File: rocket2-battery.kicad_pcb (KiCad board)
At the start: 4 copper layers, 142 parts, among them J1 Conn_01x07, J2 SMA, J3 ARM Cortex Debug, P1 PAD_SMD, P2 PAD_SMD, P3 PAD_SMD, P4 PAD_SMD, P5 PAD_SMD, P6 PAD_SMD, P7 PAD_SMD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

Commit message: Squished
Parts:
- U1: value ~ -> 3V3 LDO
- moved C26 14.6 mm to (127.9, 109.3)
- moved C27 14.6 mm to (131.5, 109.3)
- moved C28 14.6 mm to (135.4, 109.3)
- moved D15 14.6 mm to (139.3, 112.8)
- moved R46 14.6 mm to (136.3, 111.9)
- moved R47 14.6 mm to (130.3, 112.4)
- moved R49 14.6 mm to (132.2, 115.1)
- moved R50 14.6 mm to (143.2, 112.8)
- moved U14 14.6 mm to (113.8, 112.8)
- moved U15 14.6 mm to (133.2, 111.7)
- moved D16 14.6 mm to (139.3, 111.0)
- moved JP6 14.6 mm to (137.9, 115.7)
- moved R48 14.6 mm to (127.9, 113.2)
- moved R51 14.6 mm to (143.1, 111.0)
- moved D14 12.5 mm to (139.3, 100.1)
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
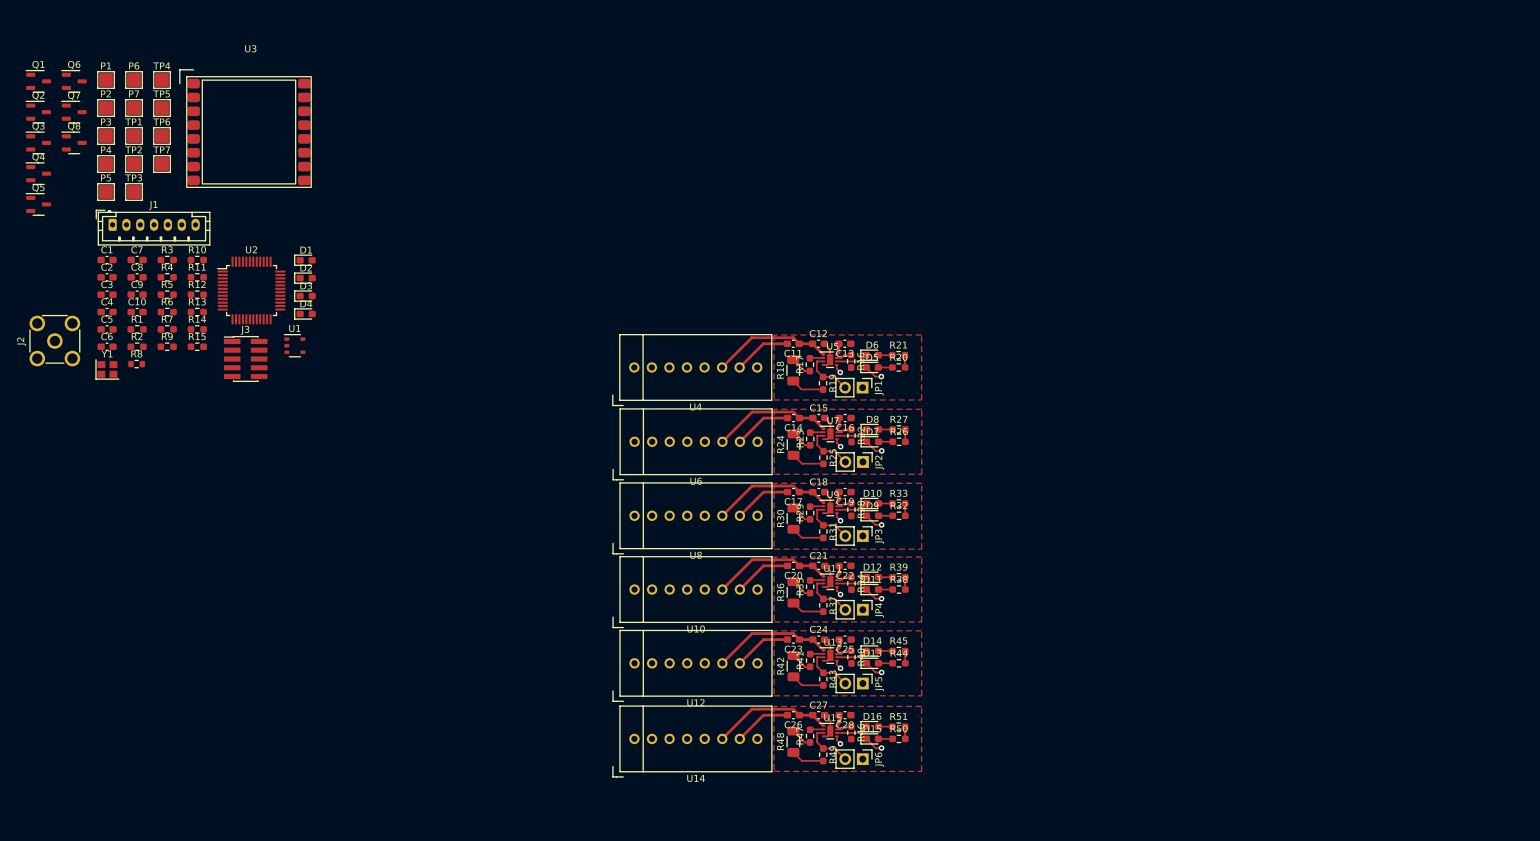
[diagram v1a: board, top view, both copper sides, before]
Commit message: mosfets done
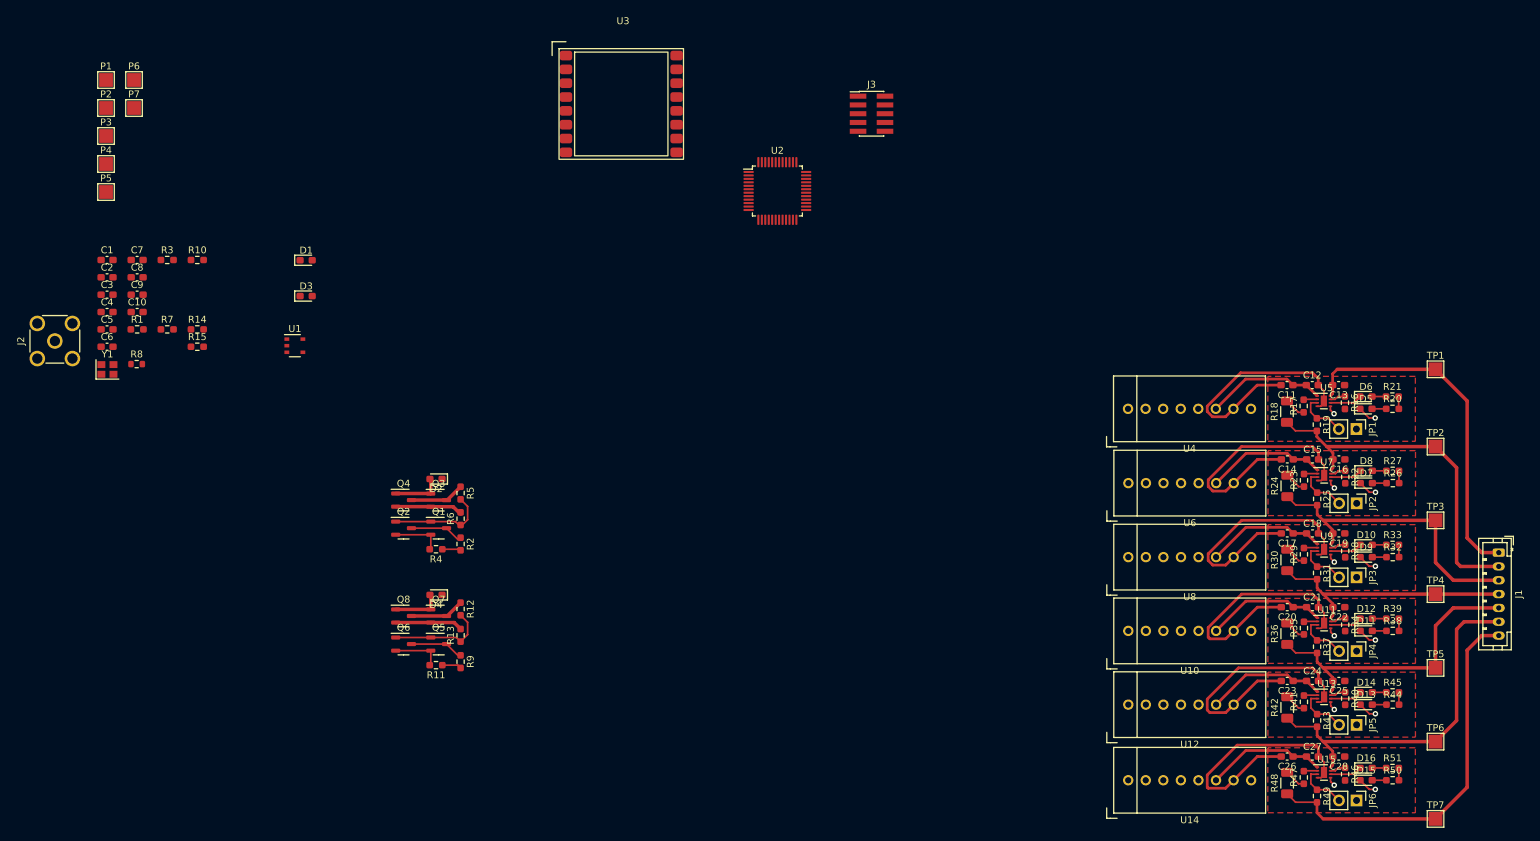
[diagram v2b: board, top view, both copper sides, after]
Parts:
- moved TP7 207.1 mm to (220.8, 124.3)
- moved J1 206.0 mm to (229.9, 85.8), turned to -90 degrees
- moved TP6 204.0 mm to (220.8, 113.2)
- moved TP5 201.2 mm to (220.8, 102.5)
- moved TP4 198.6 mm to (220.8, 91.8)
- moved TP3 194.1 mm to (220.8, 81.2)
- moved TP2 192.6 mm to (220.8, 70.5)
- moved TP1 191.2 mm to (220.8, 59.3)
- moved J3 97.2 mm to (139.2, 22.4)
- moved Q6 94.3 mm to (71.5, 99.1)
- moved Q7 89.9 mm to (76.6, 95.0)
- moved Q1 86.7 mm to (76.6, 82.3)
- moved Q5 86.0 mm to (76.6, 99.1)
- moved Q8 83.4 mm to (71.5, 95.0)
- moved Q2 80.0 mm to (71.5, 82.3)
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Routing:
- net GND: track 17.3 -> 108.1 mm
- net /Single-Cell-Charger4/ISO_GND: track 19.0 -> 89.4 mm
- net /Single-Cell-Charger/ISO_GND: track 19.0 -> 88.4 mm
- net /Single-Cell-Charger3/ISO_GND: track 19.0 -> 81.1 mm
- net /Single-Cell-Charger1/ISO_GND: track 19.0 -> 80.8 mm
- net /Single-Cell-Charger2/ISO_GND: track 19.0 -> 73.6 mm
- net /BAT_OUT+: track 1.68 -> 49.7 mm
- net Net-(Q5-D): track 0.00 -> 14.3 mm
- net Net-(Q1-D): track 0.00 -> 14.0 mm
- net Net-(Q3-G): track 0.00 -> 9.84 mm
- net Net-(Q7-G): track 0.00 -> 9.77 mm
- net +24V: track 0.00 -> 7.92 mm
- net /BATT_MAIN+: track 0.00 -> 7.91 mm
- net Net-(Q5-G): track 0.00 -> 7.24 mm
- net Net-(D2-A): track 0.00 -> 7.24 mm
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
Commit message: Almost done routing
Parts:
- removed P4: PAD_SMD, TestPoint:TestPoint_Pad_2.0x2.0mm
- R8: footprint Resistor_SMD:R_0603_1608Metric -> Resistor_SMD:R_0603_1608Metric_Pad0.98x0.95mm_HandSolder
- moved P3 199.5 mm to (202.8, 122.6)
- moved P7 194.3 mm to (198.5, 122.6)
- moved C2 188.2 mm to (209.7, 97.2)
- moved P1 184.5 mm to (189.5, 107.6)
- moved C4 182.5 mm to (207.4, 87.6)
- moved C5 182.4 mm to (207.4, 89.8)
- moved C3 181.2 mm to (201.7, 102.3), turned to 180 degrees
- moved P2 180.6 mm to (189.5, 103.4)
- moved C1 180.3 mm to (198.6, 103.6), turned to 90 degrees
- moved C8 180.1 mm to (205.6, 97.2)
- moved R3 179.9 mm to (209.7, 95.1), turned to 180 degrees
- moved C6 178.2 mm to (204.2, 86.6), turned to 90 degrees
- moved R8 177.6 mm to (207.4, 91.8)
- moved P6 174.7 mm to (189.5, 94.2)
- moved Y1 174.5 mm to (201.3, 85.1), turned to 180 degrees
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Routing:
- net GND: track 108.1 -> 212.6 mm, vias 0 -> 10
- net +24V: track 7.92 -> 74.8 mm
- net +3.3V: track 0.00 -> 23.5 mm, vias 0 -> 10
- net /BATT_MAIN+: track 7.91 -> 28.4 mm
- net /MAIN+: track 0.00 -> 15.0 mm
- net MCU_TDI: track 0.00 -> 12.5 mm, vias 0 -> 2
- net MCU_TDO: track 0.00 -> 11.3 mm
- net MCU_TMS: track 0.00 -> 9.16 mm
- net MCU_TCK: track 0.00 -> 8.98 mm
- net MCU_~{RST}: track 0.00 -> 8.50 mm
- net V_SENSE1: track 0.00 -> 6.11 mm
- net V_SENSE2: track 0.00 -> 4.70 mm
- net Net-(U2-PB8): track 0.00 -> 2.82 mm
- net Net-(U2-PD0): track 0.00 -> 2.78 mm
- net Net-(D3-A): track 0.00 -> 2.32 mm
- added copper zone on In1.Cu, net +3.3V
- added copper zone on B.Cu, net GND

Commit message: Finished most of layout
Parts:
- moved C10 0.51 mm to (206.2, 59.9)
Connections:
- U2 pad 10: MOSFET1 -> unconnected-(U2-PA0-Pad10)
- U2 pad 11: MOSFET2 -> MOSFET1
- U2 pad 12: unconnected-(U2-PA2-Pad12) -> MOSFET2
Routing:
- net GND: track 212.6 -> 328.9 mm, vias 10 -> 65
- net +24V: track 74.8 -> 137.0 mm, vias 0 -> 3
- net RADIO_DIO0: track 0.00 -> 59.8 mm, vias 0 -> 2
- net MOSFET1: track 2.81 -> 60.3 mm, vias 0 -> 2
- net RADIO_DIO2: track 0.00 -> 55.5 mm, vias 0 -> 2
- net RADIO_DIO1: track 0.00 -> 55.3 mm, vias 0 -> 2
- net RADIO_DIO3: track 0.00 -> 51.4 mm, vias 0 -> 2
- net MOSFET2: track 2.81 -> 54.0 mm, vias 0 -> 2
- net RADIO_DIO4: track 0.00 -> 50.5 mm, vias 0 -> 2
- net RADIO_nRST: track 0.00 -> 38.9 mm, vias 0 -> 2
- net +3.3V: track 23.5 -> 51.2 mm, vias 10 -> 12
- net RADIO_nCS: track 0.00 -> 27.6 mm, vias 0 -> 2
- net Net-(J2-In): track 0.00 -> 27.2 mm
- net RADIO_DIO5: track 0.00 -> 27.0 mm, vias 0 -> 2
- net RADIO_SCK: track 0.00 -> 26.4 mm, vias 0 -> 2
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- added copper zone on B.Cu, net /Single-Cell-Charger/ISO_GND
- added copper zone on B.Cu, net /Single-Cell-Charger1/ISO_GND
- added copper zone on B.Cu, net /Single-Cell-Charger2/ISO_GND
- added copper zone on B.Cu, net /Single-Cell-Charger3/ISO_GND
- added copper zone on B.Cu, net /Single-Cell-Charger4/ISO_GND
- added copper zone on In1.Cu, net GND
- added copper zone on In2.Cu, net GND

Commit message: Finished; Passed DRC
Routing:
- net GND: vias 65 -> 66
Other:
- board outline added: 91.4 x 69.8 mm
- board text added: "24V"
- board text added: "BAT+"
- board text added: "CELL 1"
- board text added: "CELL 2"
- board text added: "CELL 3"
- board text added: "CELL 4"
- board text added: "CELL 5"
- board text added: "CELL 6"
- board text added: "GND"
- board text added: "MAIN OUT"

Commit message: Daniel suggestions; Fixed charger part
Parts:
- moved C10 18.8 mm to (191.3, 71.4), turned to 180 degrees
- moved J2 12.8 mm to (189.3, 63.4), turned to 90 degrees
- moved U3 2.67 mm to (203.6, 70.4), turned to 180 degrees
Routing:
- net GND: track 328.9 -> 225.4 mm, vias 66 -> 46
- net RADIO_DIO0: track 59.8 -> 3.84 mm, vias 2 -> 1
- net RADIO_DIO1: track 55.3 -> 2.77 mm, vias 2 -> 1
- net RADIO_DIO2: track 55.5 -> 3.77 mm, vias 2 -> 1
- net RADIO_DIO3: track 51.4 -> 3.28 mm, vias 2 -> 1
- net RADIO_DIO4: track 50.5 -> 2.66 mm, vias 2 -> 1
- net /Single-Cell-Charger4/ISO_GND: track 98.9 -> 62.3 mm
- net /Single-Cell-Charger3/ISO_GND: track 90.4 -> 54.5 mm
- net /Single-Cell-Charger2/ISO_GND: track 83.0 -> 47.2 mm
- net /Single-Cell-Charger/ISO_GND: track 97.8 -> 62.6 mm
- net /Single-Cell-Charger1/ISO_GND: track 90.0 -> 54.9 mm
- net RADIO_nRST: track 38.9 -> 4.52 mm, vias 2 -> 1
- net Net-(J2-In): track 27.2 -> 0.00 mm
- net +3.3V: track 51.2 -> 25.5 mm, vias 12 -> 10
- net RADIO_DIO5: track 27.0 -> 1.54 mm, vias 2 -> 1
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- added copper zone on In2.Cu, net +3.3V
- added copper zone on In2.Cu, net /Single-Cell-Charger/ISO_5V
- added copper zone on In1.Cu, net /Single-Cell-Charger/ISO_GND
- added copper zone on In2.Cu, net /Single-Cell-Charger1/ISO_5V
- added copper zone on In1.Cu, net /Single-Cell-Charger1/ISO_GND
- added copper zone on In2.Cu, net /Single-Cell-Charger2/ISO_5V
- added copper zone on In1.Cu, net /Single-Cell-Charger2/ISO_GND
- added copper zone on In2.Cu, net /Single-Cell-Charger3/ISO_5V
- added copper zone on In1.Cu, net /Single-Cell-Charger3/ISO_GND
- added copper zone on In2.Cu, net /Single-Cell-Charger4/ISO_5V
- added copper zone on In1.Cu, net /Single-Cell-Charger4/ISO_GND
- added copper zone on In2.Cu, net /Single-Cell-Charger5/ISO_5V
- removed copper zone on In1.Cu, net +3.3V
- removed copper zone on In1.Cu, net /Single-Cell-Charger/ISO_5V
- removed copper zone on In1.Cu, net /Single-Cell-Charger1/ISO_5V
- removed copper zone on In1.Cu, net /Single-Cell-Charger2/ISO_5V
- removed copper zone on In1.Cu, net /Single-Cell-Charger3/ISO_5V
- removed copper zone on In1.Cu, net /Single-Cell-Charger4/ISO_5V
- removed copper zone on In1.Cu, net /Single-Cell-Charger5/ISO_5V
- removed copper zone on In2.Cu, net GND

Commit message: Finished
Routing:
- net RADIO_nRST: track 4.52 -> 45.5 mm, vias 1 -> 2
- net RADIO_MOSI: track 2.00 -> 37.8 mm, vias 1 -> 2
- net RADIO_DIO5: track 1.54 -> 37.2 mm, vias 1 -> 2
- net GND: track 225.4 -> 195.5 mm, vias 46 -> 71
- net RADIO_nCS: track 5.66 -> 35.0 mm, vias 1 -> 2
- net RADIO_DIO3: track 3.28 -> 32.3 mm, vias 1 -> 2
- net RADIO_SCK: track 4.45 -> 33.4 mm, vias 1 -> 2
- net RADIO_DIO0: track 3.84 -> 32.5 mm, vias 1 -> 2
- net RADIO_DIO4: track 2.66 -> 29.2 mm, vias 1 -> 2
- net RADIO_MISO: track 3.23 -> 28.9 mm, vias 1 -> 2
- net RADIO_DIO1: track 2.77 -> 26.0 mm, vias 1 -> 2
- net RADIO_DIO2: track 3.77 -> 22.8 mm, vias 1 -> 2
- net Net-(J2-In): track 0.00 -> 6.29 mm
- net /Single-Cell-Charger4/ISO_GND: track 62.3 -> 58.1 mm, vias 7 -> 8
- net /Single-Cell-Charger3/ISO_GND: track 54.5 -> 50.3 mm, vias 7 -> 8
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
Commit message: some more minor fixes
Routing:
- net GND: track 195.5 -> 192.7 mm, vias 71 -> 102
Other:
- board text added: "Battery Charge and REDS - EVAL Rocket Project Liquids - 2024"
